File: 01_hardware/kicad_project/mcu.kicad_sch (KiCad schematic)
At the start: 31 parts, among them U1 STM32G474RBT6, Y1 16MHz 9pF

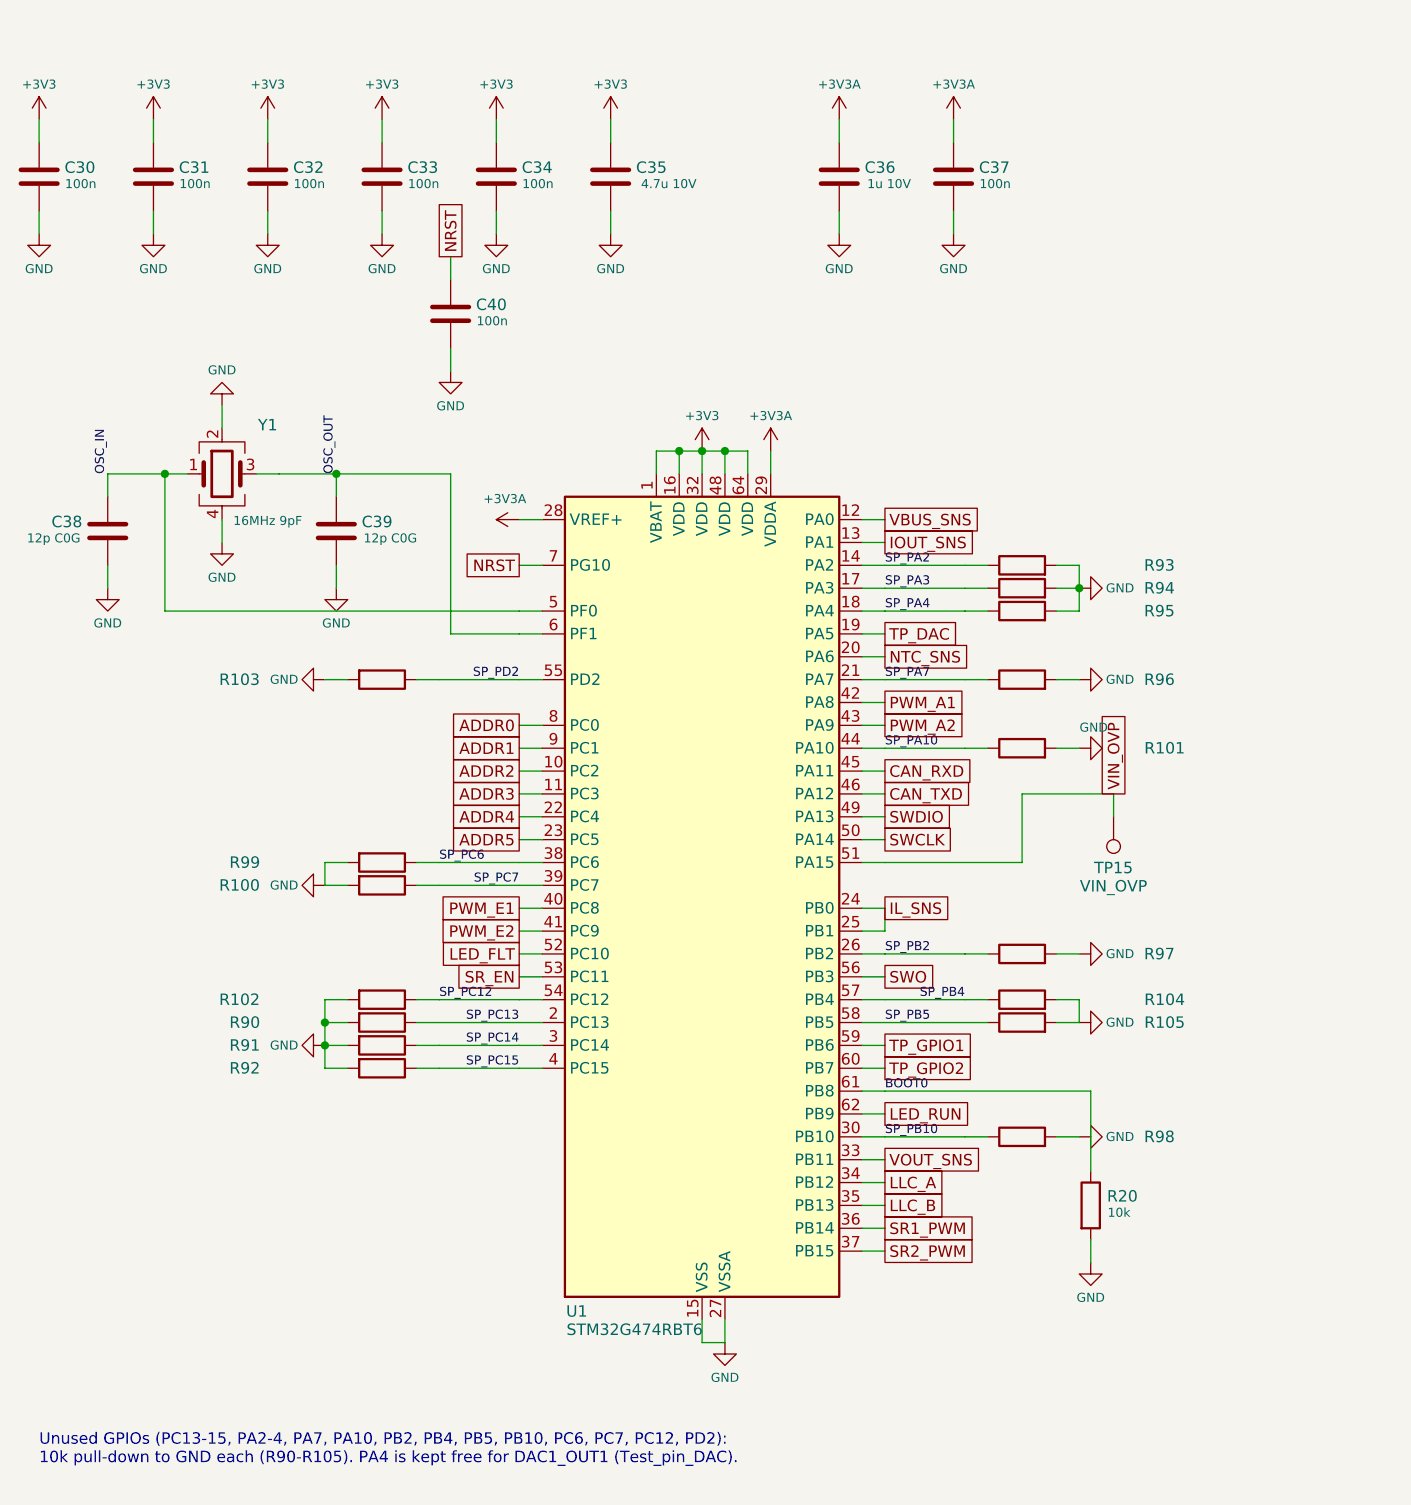
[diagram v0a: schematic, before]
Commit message: VIN monitor: sawtooth/comparator PWM over spare isolator channel to PA2 (TIM15_CH1)
- Primary: PNP current-source ramp (~5 ms) into 47 nF C0G, U17 reset detector,
  U18 PWM comparator vs OVP_DIV; R81/R82 now 0.1 %
- U12 VI2->VO2 carries VIN_PWM to PA2; R93 is its pull-down
- PCB: new block placed/routed below U15/U16, R106 moved for courtyard,
  GNDP island vias, silkscreen for new parts; DRC clean, netlist parity OK
- Outputs regenerated (BOM, Gerbers, CPL, EasyEDA, PDFs, pin-map)

Co-Authored-By: Claude Opus 5.5 <noreply@anthropic.com>
Claude-Session: https://claude.ai/code/session_01A35wrnwFKLPSaRSxxHs471
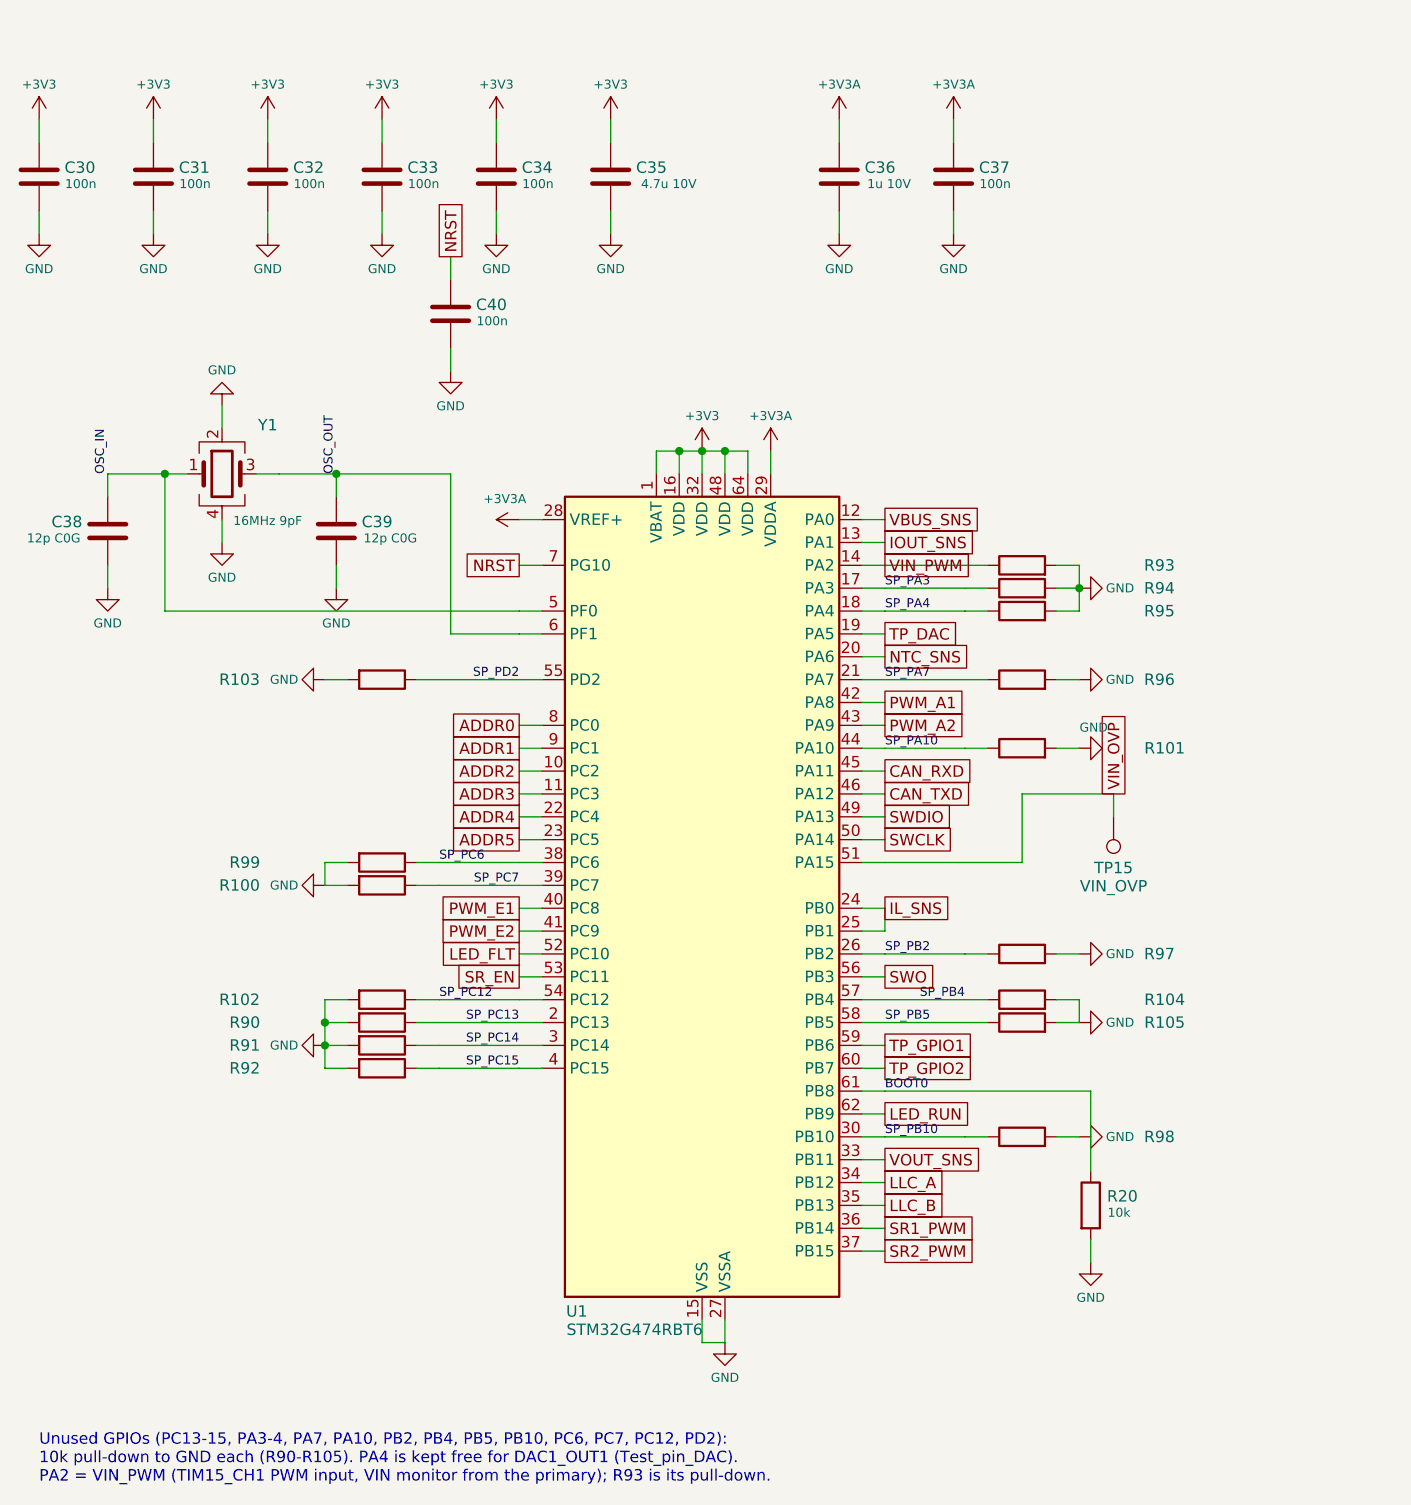
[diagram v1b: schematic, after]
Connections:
- net SP_PA2 renamed VIN_PWM
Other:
- note added: "Unused GPIOs (PC13-15, PA3-4, PA7, PA10, PB2, PB4, PB5, PB10, PC6, PC7, PC12, PD2): 10k pull-down to GND each (R90-R105). PA4 is kept free for DAC1_OUT1 (Test_pin_DAC). PA2 = VIN_PWM (TIM15_CH1 PWM input, VIN monitor from the primary); R93 is its pull-down."
- note removed: "Unused GPIOs (PC13-15, PA2-4, PA7, PA10, PB2, PB4, PB5, PB10, PC6, PC7, PC12, PD2): 10k pull-down to GND each (R90-R105). PA4 is kept free for DAC1_OUT1 (Test_pin_DAC)."
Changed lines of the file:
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@@
     (stroke (width 0) (type default))
   )
-  (text "Unused GPIOs (PC13-15, PA2-4, PA7, PA10, PB2, PB4, PB5, PB10, PC6, PC7, PC12, PD2):\n10k pull-down to GND each (R90-R105). PA4 is kept free for DAC1_OUT1 (Test_pin_DAC)."
+  (text "Unused GPIOs (PC13-15, PA3-4, PA7, PA10, PB2, PB4, PB5, PB10, PC6, PC7, PC12, PD2):\n10k pull-down to GND each (R90-R105). PA4 is kept free for DAC1_OUT1 (Test_pin_DAC).\nPA2 = VIN_PWM (TIM15_CH1 PWM input, VIN monitor from the primary); R93 is its pull-down."
     (at 129.54 203.2 0)
     (effects (font (size 1.27 1.27)) (justify left top))
   )
-  (label "SP_PA2" (at 223.52 106.68 0)
-    (effects (font (size 1.0 1.0)) (justify left bottom))
-  )
   (label "SP_PA3" (at 223.52 109.22 0)
     (effects (font (size 1.0 1.0)) (justify left bottom))
@@
       (effects (font (size 1.27 1.27)) hide)
     )
+  )
+  (global_label "VIN_PWM" (shape passive) (at 223.52 106.68 0)
+    (effects (font (size 1.27 1.27)) (justify left))
+    (property "Intersheet References" "${INTERSHEET_REFS}" (id 0) (at 223.52 106.68 0)
+      (effects (font (size 1.27 1.27)) hide)
+    )

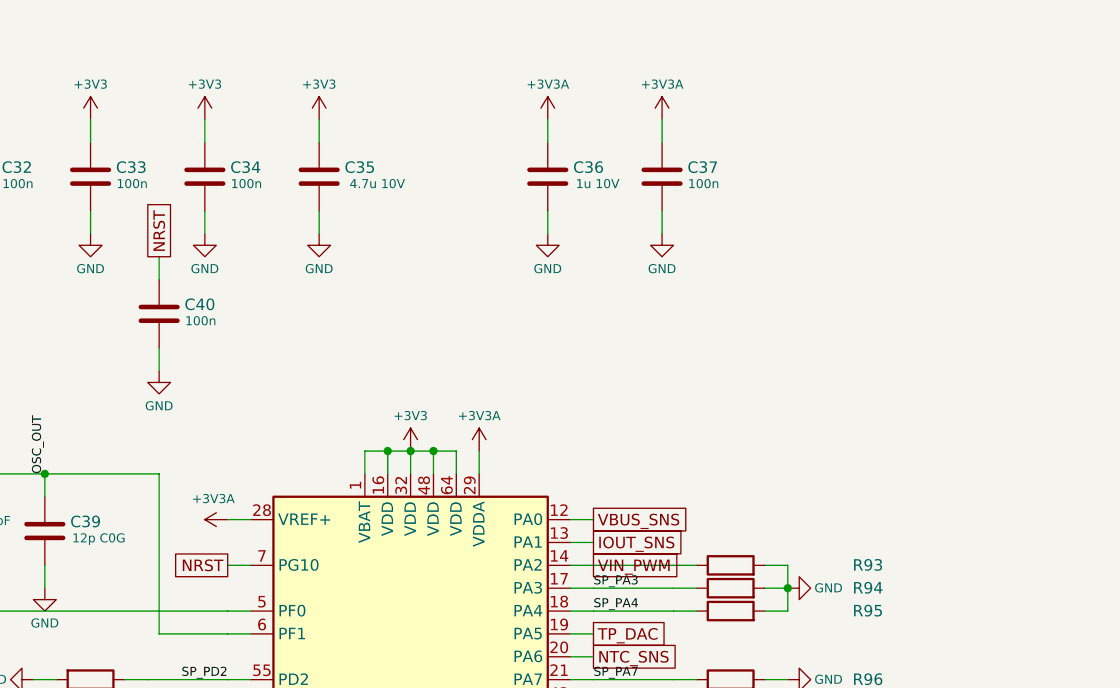
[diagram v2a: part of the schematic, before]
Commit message: External REF3030 ADC reference; full review and documentation update
- U19 REF3030AIDBZR (3.000 V +/-0.2 %, LCSC C38423) + C85 drive VREF+ (new net
  VREF_ADC); VREF+ separated from VDDA; R25 (IL zero) and R29 (NTC pull-up)
  moved to VREF_ADC so those channels are ratiometric
- Full scales: VBUS/VOUT 61.8 V, IL +/-18.75 A, IOUT 6.0 A, DAC/COMP 0-3.0 V
- PCB: U19/C85 placed and routed, pins 28/29 hand-routed; DRC clean, parity
  OK, isolation 4.0 mm
- Design notes (DOCX/PDF), root and firmware READMEs, pin-map, layout review
  image, BOM, Gerbers, CPL, EasyEDA zip and PDFs updated

Co-Authored-By: Claude Opus 5.5 <noreply@anthropic.com>
Claude-Session: https://claude.ai/code/session_01A35wrnwFKLPSaRSxxHs471
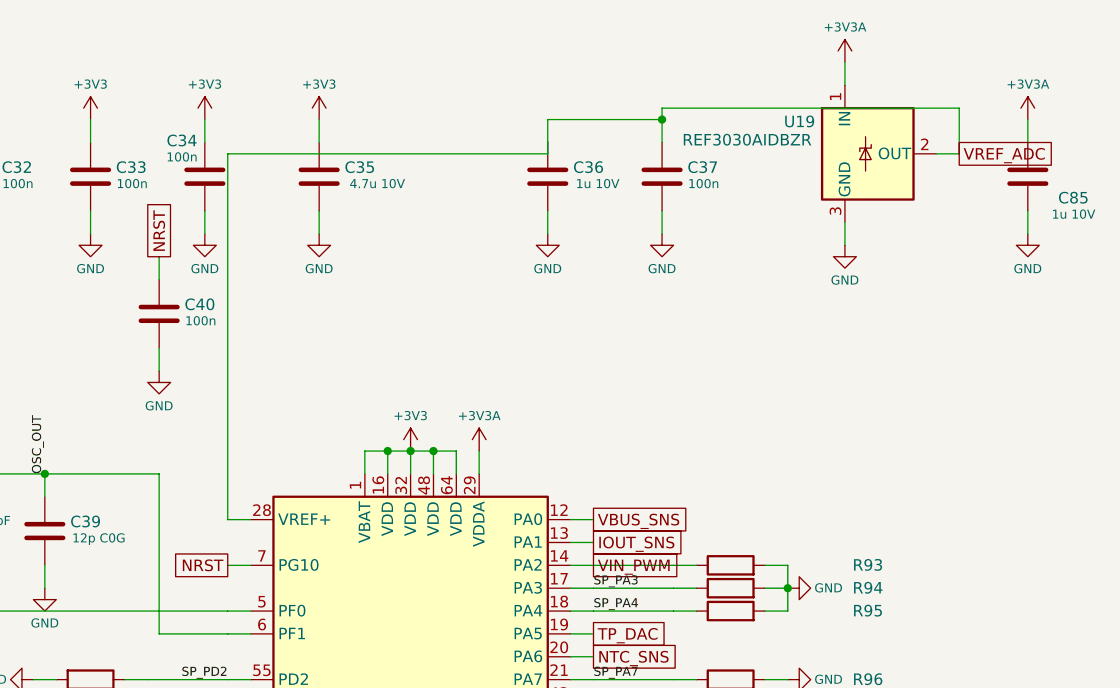
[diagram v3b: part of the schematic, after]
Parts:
- added C85: 1u 10V, Capacitor_SMD:C_0402_1005Metric, symbol Device:C
- added U19: REF3030AIDBZR, Package_TO_SOT_SMD:SOT-23, symbol Reference_Voltage:REF3030
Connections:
- net +3V3A: now also C85.1, U19.1 (IN); no longer C36.1, C37.1, U1.28 (VREF+)
- net GND: now also C85.2, U19.3 (GND)
- new net VREF_ADC: C36.1, C37.1, U1.28 (VREF+), U19.2 (OUT)

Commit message: Rev D order prep: common F1/L2/L3 parts, JLC-checked LCSC numbers, assembly files
- F1: 2512 -> 1206 7 A 63 V fuse (Littelfuse 0458007.DR, C206980; 2nd source Schurter 3413.0326.11)
- L2/L3: SRP5030 -> 5040 shielded 47 uH (SWPA5040S470MT, C86617; 2nd source SRN5040-470M, NRS5040T470MMGK)
- EN_AUX re-routed off the L2 pad gap; VIN track centred between the L3 pads (0.4 mm each side)
- LCSC numbers checked in the JLCPCB library for every assembled part (design.py JLC_LCSC),
  written to the BOMs, schematic and PCB fields
- New JLC assembly upload files DCDC_JLC_BOM.csv / DCDC_JLC_CPL.csv (217 parts; U1, T1,
  connectors, headers and SW1 hand-soldered) and jlc_order_files.py to rebuild them
- 03_calculations/aux_fuse_check.py: aux inductor peak 0.27 A vs 1.1 A Isat; F1 4.8 A at 12 V / 50 W
- Design notes (docx/pdf), README, Gerbers, CPL, PDFs and DRC report regenerated
- Checks: DRC (JLC rules) 0 errors / 0 unconnected, netlist 134 nets / 257 parts 0 errors,
  isolation check 0 errors, silkscreen clean

Co-Authored-By: Claude Opus 5.5 <noreply@anthropic.com>
Claude-Session: https://claude.ai/code/session_01A35wrnwFKLPSaRSxxHs471
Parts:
- C30, C31, C32, C33, C34, C37, C40: LCSC (none) -> C1525
- C35: LCSC (none) -> C19666
- C36, C85: LCSC (none) -> C52923
- C38, C39: LCSC (none) -> C1547
- R100, R101, R102, R103, R104, R20, R90, R91, R92, R93, R94, R95, R96, R97, R98, R99: LCSC (none) -> C25744
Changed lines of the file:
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@@
       (effects (font (size 1.27 1.27)) hide)
     )
-    (property "LCSC" "" (id 4) (at 129.54 63.5 0)
+    (property "LCSC" "C1525" (id 4) (at 129.54 63.5 0)
       (effects (font (size 1.27 1.27)) hide)
     )
@@
       (effects (font (size 1.27 1.27)) hide)
     )
-    (property "LCSC" "" (id 4) (at 142.24 63.5 0)
+    (property "LCSC" "C1525" (id 4) (at 142.24 63.5 0)
       (effects (font (size 1.27 1.27)) hide)
     )
@@
       (effects (font (size 1.27 1.27)) hide)
     )
-    (property "LCSC" "" (id 4) (at 154.94 63.5 0)
+    (property "LCSC" "C1525" (id 4) (at 154.94 63.5 0)
       (effects (font (size 1.27 1.27)) hide)
     )
@@
       (effects (font (size 1.27 1.27)) hide)
     )
-    (property "LCSC" "" (id 4) (at 167.64 63.5 0)
+    (property "LCSC" "C1525" (id 4) (at 167.64 63.5 0)
       (effects (font (size 1.27 1.27)) hide)
     )
@@
       (effects (font (size 1.27 1.27)) hide)
     )
-    (property "LCSC" "" (id 4) (at 180.34 63.5 0)
+    (property "LCSC" "C1525" (id 4) (at 180.34 63.5 0)
       (effects (font (size 1.27 1.27)) hide)
     )
@@
       (effects (font (size 1.27 1.27)) hide)
     )
-    (property "LCSC" "" (id 4) (at 193.04 63.5 0)
+    (property "LCSC" "C19666" (id 4) (at 193.04 63.5 0)
       (effects (font (size 1.27 1.27)) hide)
     )
@@
       (effects (font (size 1.27 1.27)) hide)
     )
-    (property "LCSC" "" (id 4) (at 218.44 63.5 0)
+    (property "LCSC" "C52923" (id 4) (at 218.44 63.5 0)
       (effects (font (size 1.27 1.27)) hide)
     )
@@
       (effects (font (size 1.27 1.27)) hide)
     )
-    (property "LCSC" "" (id 4) (at 231.14 63.5 0)
+    (property "LCSC" "C1525" (id 4) (at 231.14 63.5 0)
       (effects (font (size 1.27 1.27)) hide)
     )
@@
       (effects (font (size 1.27 1.27)) hide)
     )
-    (property "LCSC" "" (id 4) (at 271.78 63.5 0)
+    (property "LCSC" "C52923" (id 4) (at 271.78 63.5 0)
       (effects (font (size 1.27 1.27)) hide)
     )
@@
       (effects (font (size 1.27 1.27)) hide)
     )
-    (property "LCSC" "" (id 4) (at 137.16 102.87 0)
+    (property "LCSC" "C1547" (id 4) (at 137.16 102.87 0)
       (effects (font (size 1.27 1.27)) hide)
     )
@@
       (effects (font (size 1.27 1.27)) hide)
     )
-    (property "LCSC" "" (id 4) (at 162.56 102.87 0)
+    (property "LCSC" "C1547" (id 4) (at 162.56 102.87 0)
       (effects (font (size 1.27 1.27)) hide)
     )
@@
       (effects (font (size 1.27 1.27)) hide)
     )
-    (property "LCSC" "" (id 4) (at 175.26 78.74 0)
+    (property "LCSC" "C1525" (id 4) (at 175.26 78.74 0)
       (effects (font (size 1.27 1.27)) hide)
     )
@@
       (effects (font (size 1.27 1.27)) hide)
     )
-    (property "LCSC" "" (id 4) (at 246.38 177.8 0)
+    (property "LCSC" "C25744" (id 4) (at 246.38 177.8 0)
       (effects (font (size 1.27 1.27)) hide)
     )
@@
       (effects (font (size 1.27 1.27)) hide)
     )
-    (property "LCSC" "" (id 4) (at 167.64 157.48 0)
+    (property "LCSC" "C25744" (id 4) (at 167.64 157.48 0)
       (effects (font (size 1.27 1.27)) hide)
     )
@@
       (effects (font (size 1.27 1.27)) hide)
     )
-    (property "LCSC" "" (id 4) (at 167.64 160.02 0)
+    (property "LCSC" "C25744" (id 4) (at 167.64 160.02 0)
       (effects (font (size 1.27 1.27)) hide)
     )
@@
       (effects (font (size 1.27 1.27)) hide)
     )
-    (property "LCSC" "" (id 4) (at 167.64 162.56 0)
+    (property "LCSC" "C25744" (id 4) (at 167.64 162.56 0)
       (effects (font (size 1.27 1.27)) hide)
     )
@@
       (effects (font (size 1.27 1.27)) hide)
     )
-    (property "LCSC" "" (id 4) (at 238.76 106.68 0)
+    (property "LCSC" "C25744" (id 4) (at 238.76 106.68 0)
       (effects (font (size 1.27 1.27)) hide)
     )
@@
       (effects (font (size 1.27 1.27)) hide)
     )
-    (property "LCSC" "" (id 4) (at 238.76 109.22 0)
+    (property "LCSC" "C25744" (id 4) (at 238.76 109.22 0)
       (effects (font (size 1.27 1.27)) hide)
     )
@@
       (effects (font (size 1.27 1.27)) hide)
     )
-    (property "LCSC" "" (id 4) (at 238.76 111.76 0)
+    (property "LCSC" "C25744" (id 4) (at 238.76 111.76 0)
       (effects (font (size 1.27 1.27)) hide)
     )
@@
       (effects (font (size 1.27 1.27)) hide)
     )
-    (property "LCSC" "" (id 4) (at 238.76 119.38 0)
+    (property "LCSC" "C25744" (id 4) (at 238.76 119.38 0)
       (effects (font (size 1.27 1.27)) hide)
     )
@@
       (effects (font (size 1.27 1.27)) hide)
     )
-    (property "LCSC" "" (id 4) (at 238.76 149.86 0)
+    (property "LCSC" "C25744" (id 4) (at 238.76 149.86 0)
       (effects (font (size 1.27 1.27)) hide)
     )
@@
       (effects (font (size 1.27 1.27)) hide)
     )
-    (property "LCSC" "" (id 4) (at 238.76 170.18 0)
+    (property "LCSC" "C25744" (id 4) (at 238.76 170.18 0)
       (effects (font (size 1.27 1.27)) hide)
     )
@@
       (effects (font (size 1.27 1.27)) hide)
     )
-    (property "LCSC" "" (id 4) (at 167.64 139.7 0)
+    (property "LCSC" "C25744" (id 4) (at 167.64 139.7 0)
       (effects (font (size 1.27 1.27)) hide)
     )
@@
       (effects (font (size 1.27 1.27)) hide)
     )
-    (property "LCSC" "" (id 4) (at 167.64 142.24 0)
+    (property "LCSC" "C25744" (id 4) (at 167.64 142.24 0)
       (effects (font (size 1.27 1.27)) hide)
     )
@@
       (effects (font (size 1.27 1.27)) hide)
     )
-    (property "LCSC" "" (id 4) (at 238.76 127.0 0)
+    (property "LCSC" "C25744" (id 4) (at 238.76 127.0 0)
       (effects (font (size 1.27 1.27)) hide)
     )
@@
       (effects (font (size 1.27 1.27)) hide)
     )
-    (property "LCSC" "" (id 4) (at 167.64 154.94 0)
+    (property "LCSC" "C25744" (id 4) (at 167.64 154.94 0)
       (effects (font (size 1.27 1.27)) hide)
     )
@@
       (effects (font (size 1.27 1.27)) hide)
     )
-    (property "LCSC" "" (id 4) (at 167.64 119.38 0)
+    (property "LCSC" "C25744" (id 4) (at 167.64 119.38 0)
       (effects (font (size 1.27 1.27)) hide)
     )
@@
       (effects (font (size 1.27 1.27)) hide)
     )
-    (property "LCSC" "" (id 4) (at 238.76 154.94 0)
-      (effects (font (size 1.27 1.27)) hide)
-    )
+    (property "LCSC" "C25744" (id 4) (at 238.76 154.94 0)
+      (effects (font (size 1.27 1.27)) hide)
+    )
